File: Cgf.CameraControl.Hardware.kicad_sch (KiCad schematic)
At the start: 29 parts, among them J1 5V input, J2 AudioJack3, J3 Pan, J4 Tilt, J5 Sens, J6 Prog, Q1 BSS123, Q2 2N7002K, Q3 2N7002K, Q4 MUN5211DW1, U1 WT32-ETH01, U2 DRV8212P, U3 DRV8212P

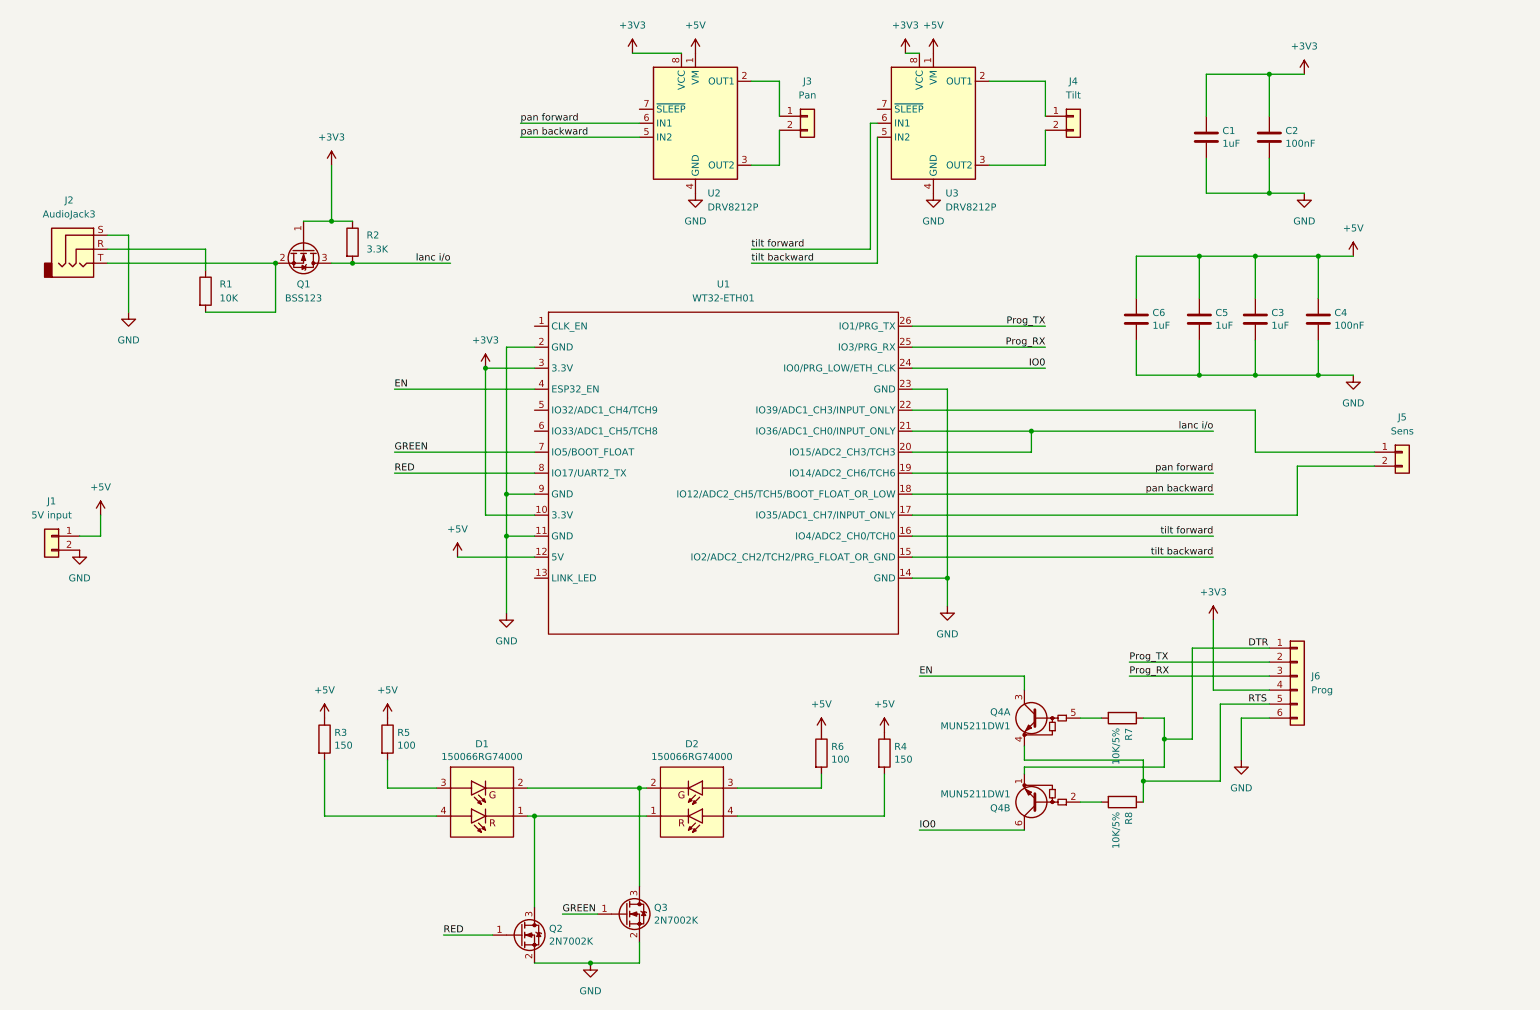
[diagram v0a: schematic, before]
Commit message: make sure all parts have footprints and also simplify led circuit
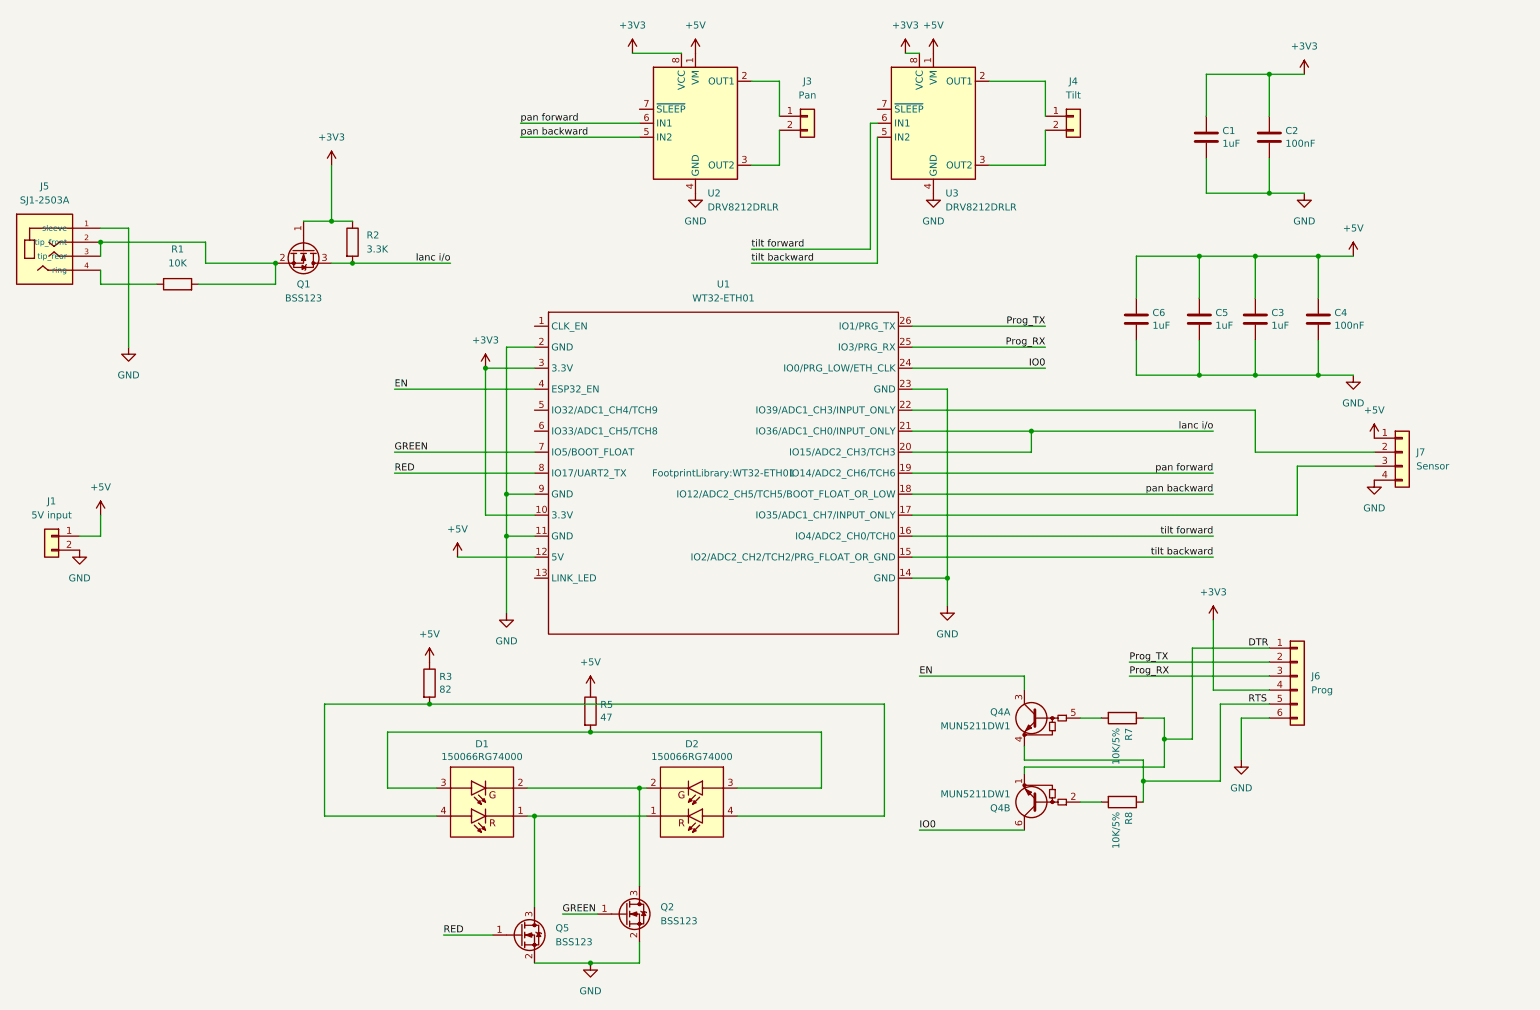
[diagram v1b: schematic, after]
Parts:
- removed J2: AudioJack3, symbol Connector_Audio:AudioJack3
- removed J5: Sens, symbol Connector_Generic:Conn_01x02
- removed Q2, Q3: 2N7002K, Package_TO_SOT_SMD:SOT-23, symbol Transistor_FET:2N7002K
- removed R4: 150, Resistor_SMD:R_1206_3216Metric, symbol Device:R
- removed R6: 100, Resistor_SMD:R_1206_3216Metric, symbol Device:R
- added J5: SJ1-2503A, FootprintLibrary:CUI_SJ1-2503A, symbol SymbolLibrary:SJ1-2503A
- added J7: Sensor, Connector_PinHeader_2.54mm:PinHeader_1x04_P2.54mm_Vertical, symbol Connector_Generic:Conn_01x04
- added Q2, Q5: BSS123, Package_TO_SOT_SMD:SOT-23, symbol Transistor_FET:BSS123
- D1, D2: footprint Project:150066RG74000 -> FootprintLibrary:SMT_RG74000_WRE
- J1, J3, J4: footprint (none) -> Connector_PinHeader_2.54mm:PinHeader_1x02_P2.54mm_Vertical
- J6: footprint (none) -> Connector_PinHeader_2.54mm:PinHeader_1x06_P2.54mm_Vertical
- R1, R2: footprint (none) -> Resistor_SMD:R_1206_3216Metric
- R3: value 150 -> 82
- R5: value 100 -> 47
- U1: footprint WT32-ETH01:WT32-ETH01 -> FootprintLibrary:WT32-ETH01
- U2, U3: value DRV8212P -> DRV8212DRLR; footprint Package_SON:WSON-8-1EP_2x2mm_P0.5mm_EP0.9x1.6mm_ThermalVias -> Package_TO_SOT_SMD:SOT-563
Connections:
- net +5V: now also J7.1 (Pin_1)
- net GND: now also J5.1 (sleeve), J7.4 (Pin_4), Q2.2 (S), Q5.2 (S)
- net GREEN: now also Q2.1 (G)
- net RED: now also Q5.1 (G)
- net at D1.2, D2.2: now also Q2.3 (D)
- net at R1.1: now also J5.4 (ring)
- net at Q1.2 (S), R1.2: now also J5.2 (tip_front), J5.3 (tip_rear)
- net at D1.1, D2.1: now also Q5.3 (D)
- net at D1.3, R5.2: now also D2.3
- net at D1.4, R3.2: now also D2.4
- net at U1.17 (IO35/ADC1_CH7/INPUT_ONLY): now also J7.3 (Pin_3)
- net at U1.22 (IO39/ADC1_CH3/INPUT_ONLY): now also J7.2 (Pin_2)
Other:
- moved on the sheet: R1

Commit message: update schematic with suggestions
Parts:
- removed Q1: BSS123, Package_TO_SOT_SMD:SOT-23, symbol Transistor_FET:BSS123
- removed R1: 10K, Resistor_SMD:R_1206_3216Metric, symbol Device:R
- removed R2: 3.3K, Resistor_SMD:R_1206_3216Metric, symbol Device:R
- removed U2, U3: DRV8212DRLR, Package_TO_SOT_SMD:SOT-563, symbol Driver_Motor:DRV8212P
- added R4: 150, Resistor_SMD:R_0805_2012Metric, symbol Device:R
- added R6: 100, Resistor_SMD:R_0805_2012Metric, symbol Device:R
- added U2, U4: DRV8212DRLR, FootprintLibrary:SOT6_DRV8212_TEX, symbol SymbolLibrary:DRV8212DRLR
- added U3: TXS0102DCT, Package_SO:SSOP-8_2.95x2.8mm_P0.65mm, symbol Logic_LevelTranslator:TXS0102DCT
- added U5: TXS0101DCK, Package_TO_SOT_SMD:SOT-363_SC-70-6, symbol Logic_LevelTranslator:TXS0101DCK
- C1, C2, C3, C4, C5, C6: footprint Capacitor_SMD:C_1206_3216Metric -> Capacitor_SMD:C_0805_2012Metric
- R3: value 82 -> 150; footprint Resistor_SMD:R_1206_3216Metric -> Resistor_SMD:R_0805_2012Metric
- R5: value 47 -> 100; footprint Resistor_SMD:R_1206_3216Metric -> Resistor_SMD:R_0805_2012Metric
- R7, R8: footprint Resistor_SMD:R_1206_3216Metric -> Resistor_SMD:R_0805_2012Metric
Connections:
- net +3V3: now also U3.3 (VCCA), U3.6 (OE), U5.1 (V_{CCA}), U5.5 (OE)
- net +5V: now also R4.1, R6.1, U2.5 (VM), U3.7 (VCCB), U4.5 (VM)
- net GND: now also U2.3 (GND), U3.2 (GND), U4.3 (GND), U5.2 (GND)
- net lanc i/o: now also U5.3 (A)
- net pan backward: now also U4.2 (IN2)
- net pan forward: now also U4.1 (IN1)
- net tilt backward: now also U2.2 (IN2)
- net tilt forward: now also U2.1 (IN1)
- net at J4.1 (Pin_1): now also U2.6 (OUT1)
- net at J4.2 (Pin_2): now also U2.4 (OUT2)
- net at J3.1 (Pin_1): now also U4.6 (OUT1)
- net at J3.2 (Pin_2): now also U4.4 (OUT2)
- net at D1.4, R3.2: no longer D2.4
- net at J5.2 (tip_front), J5.3 (tip_rear): now also U5.4 (B)
- net at J5.4 (ring): now also U5.6 (V_{CCB})
- net at D1.3, R5.2: no longer D2.3
- net at U1.17 (IO35/ADC1_CH7/INPUT_ONLY): now also U3.4 (A2); no longer J7.3 (Pin_3)
- net at U1.22 (IO39/ADC1_CH3/INPUT_ONLY): now also U3.5 (A1); no longer J7.2 (Pin_2)
- new net: D2.4, R4.2
- new net: D2.3, R6.2
- new net: J7.2 (Pin_2), U3.8 (B1)
- new net: J7.3 (Pin_3), U3.1 (B2)
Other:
- moved on the sheet: C3, C4, C5, C6, J3, J4, J7, R3, R5

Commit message: Apply suggestions from review
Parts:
- removed U3: TXS0102DCT, Package_SO:SSOP-8_2.95x2.8mm_P0.65mm, symbol Logic_LevelTranslator:TXS0102DCT
- removed U5: TXS0101DCK, Package_TO_SOT_SMD:SOT-363_SC-70-6, symbol Logic_LevelTranslator:TXS0101DCK
- added Q1: BSS123, Package_TO_SOT_SMD:SOT-23, symbol Transistor_FET:BSS123
- added R1: 10K, Resistor_SMD:R_0805_2012Metric, symbol Device:R
- added R2: 3.3K, Resistor_SMD:R_0805_2012Metric, symbol Device:R
- added U5: 74LVC2T45DC, Package_SO:VSSOP-8_2.3x2mm_P0.5mm, symbol Logic_LevelTranslator:74LVC2T45DC
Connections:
- net +3V3: now also Q1.1 (G), R2.1, U5.1 (VCCA)
- net +5V: now also U5.8 (VCCB)
- net GND: now also U5.4 (GND), U5.5 (DIR)
- net lanc i/o: now also Q1.2 (S), R2.2
- net at J5.2 (tip_front), J5.3 (tip_rear): now also Q1.3 (D), R1.1
- net at J5.4 (ring): now also R1.2
- net at U1.17 (IO35/ADC1_CH7/INPUT_ONLY): now also U5.3 (2A)
- net at U1.22 (IO39/ADC1_CH3/INPUT_ONLY): now also U5.2 (1A)
- net at J7.2 (Pin_2): now also U5.7 (1B)
- net at J7.3 (Pin_3): now also U5.6 (2B)
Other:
- moved on the sheet: C1, C2, C3, C4, C5, C6

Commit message: replace footprint after the pcb failed validation
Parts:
- U5: footprint Package_SO:VSSOP-8_2.3x2mm_P0.5mm -> FootprintLibrary:VSSOP8_74LVC2T45DC_125_NEX-L
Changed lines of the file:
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@@
 			)
 		)
-		(property "Footprint" "Package_SO:VSSOP-8_2.3x2mm_P0.5mm"
+		(property "Footprint" "FootprintLibrary:VSSOP8_74LVC2T45DC_125_NEX-L"
 			(at 251.46 116.84 0)
 			(effects
